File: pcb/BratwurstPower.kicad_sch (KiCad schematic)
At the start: 36 parts, among them J1 BarrelJack, J10 GPIO, J2 Raspi, J3 USB1in, J4 USB1out, J5 I2C, J6 I2C, J7 USB2in, J8 USB2out, J9 EXT, Q1 AO3401A, U1 PCA9557PW

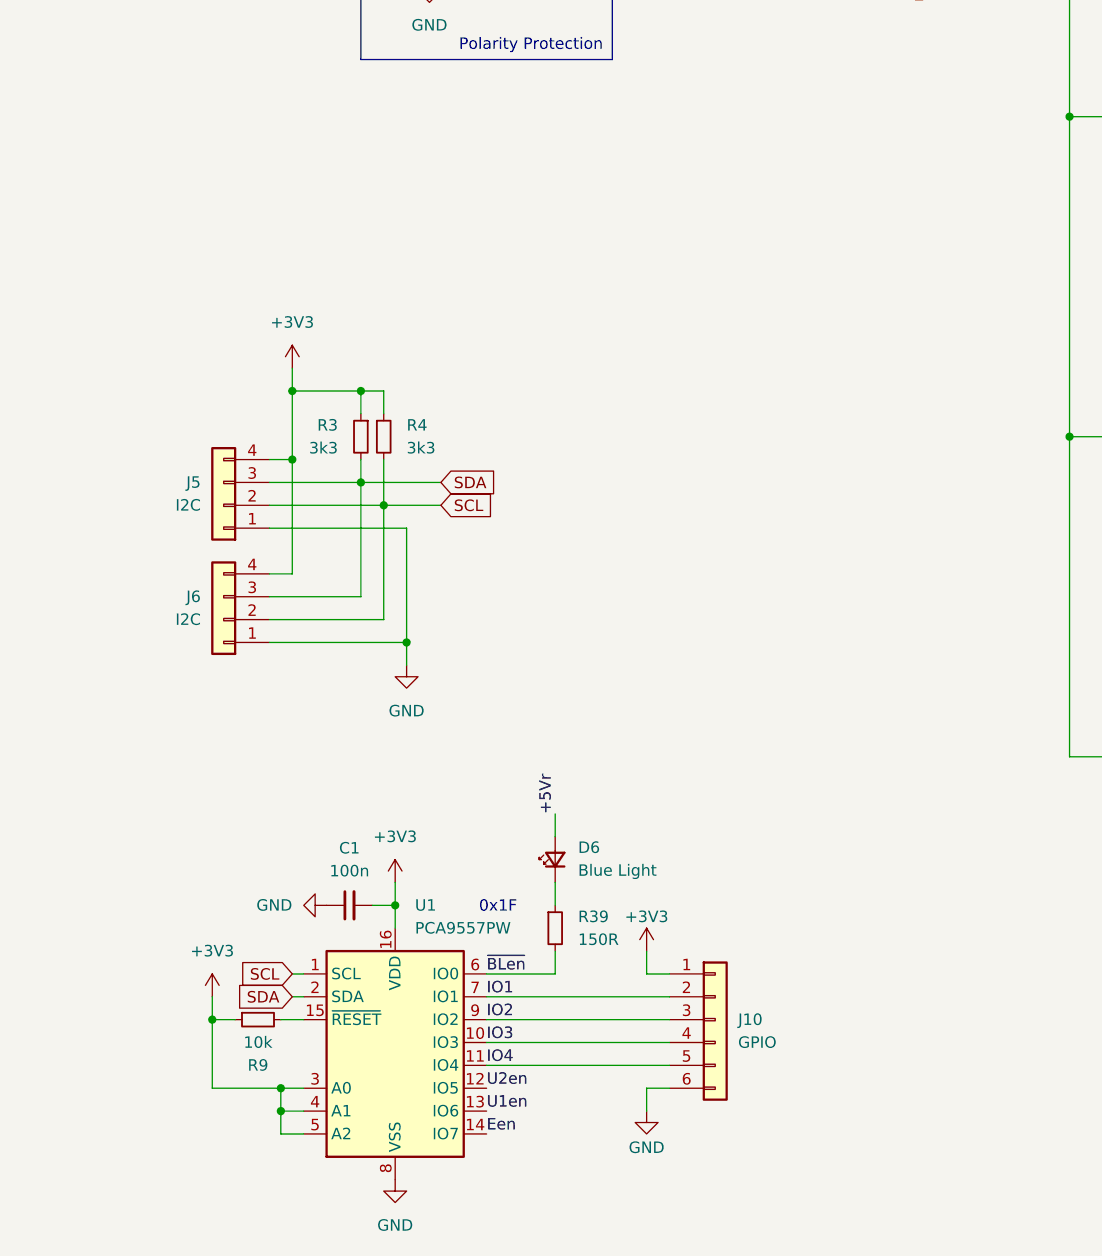
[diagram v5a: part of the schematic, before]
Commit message: fix: I2C pull-up strength
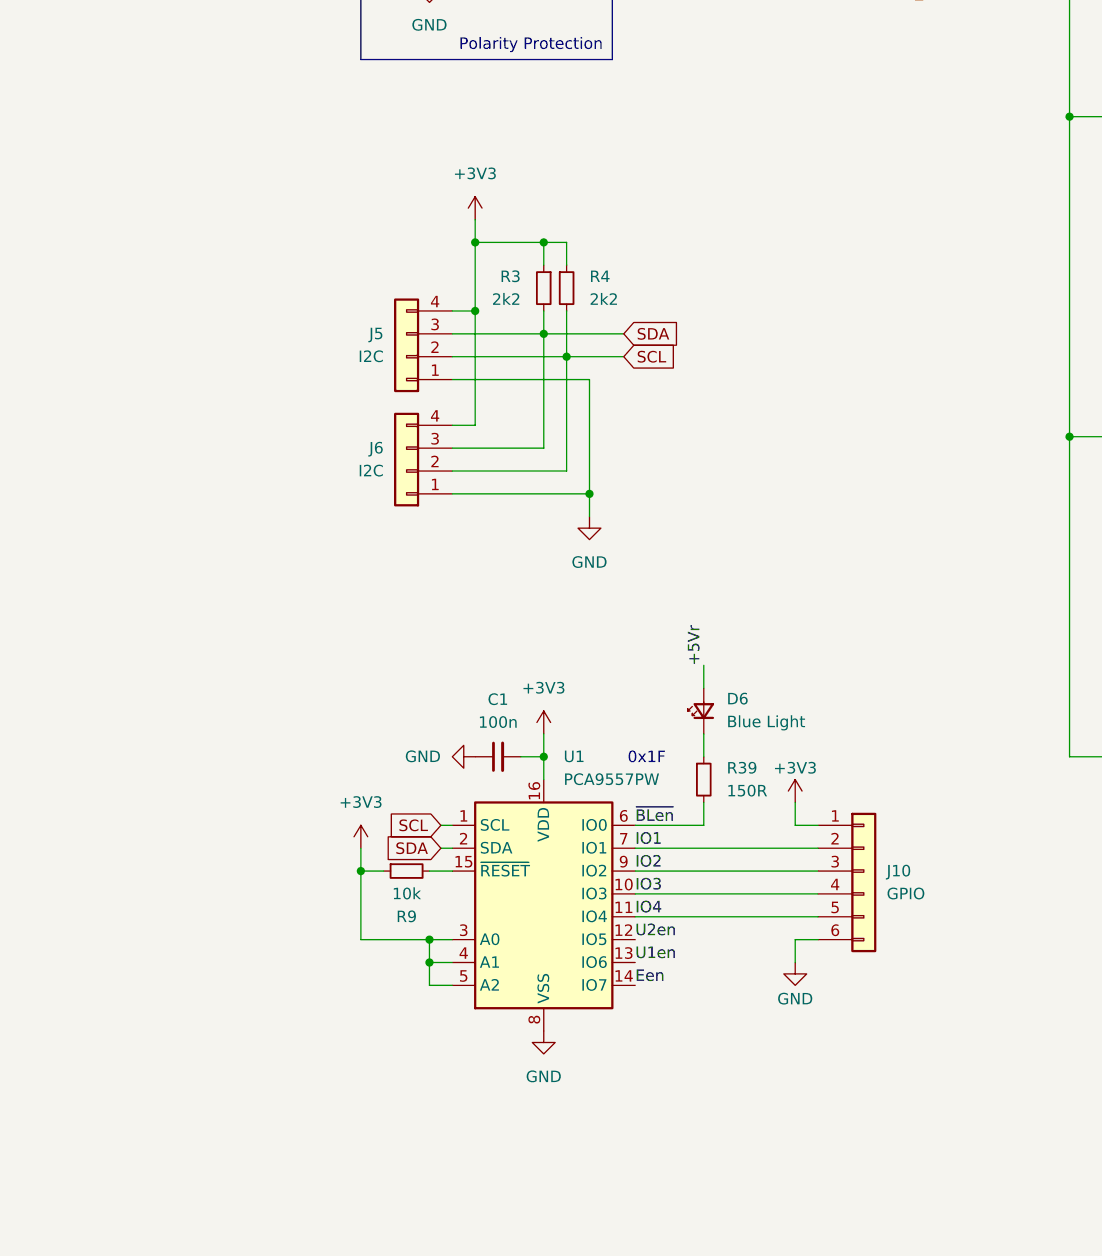
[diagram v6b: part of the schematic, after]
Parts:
- R3, R4: value 3k3 -> 2k2
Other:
- moved on the sheet: C1, D6, J10, J5, J6, R3, R39, R4, R9, U1

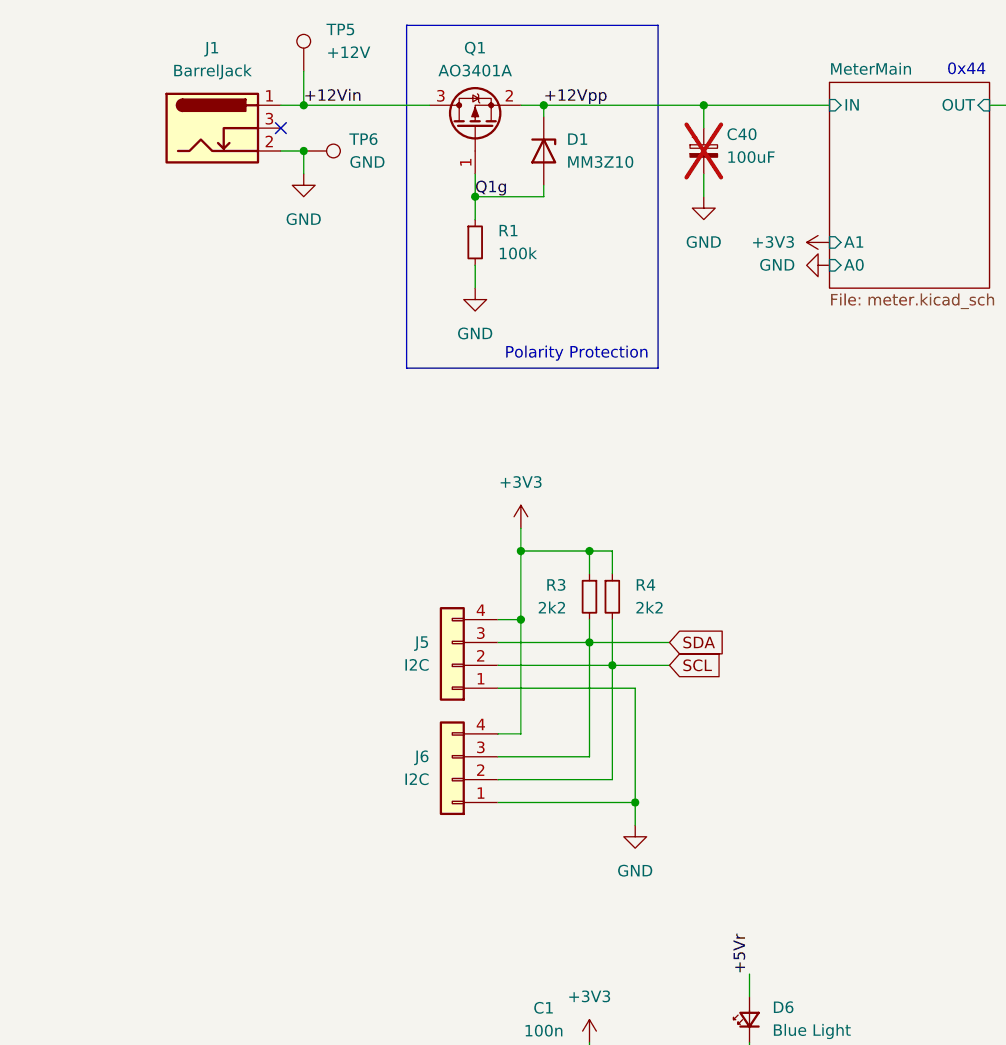
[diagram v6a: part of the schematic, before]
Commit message: feat: polarity protection for I2C bus
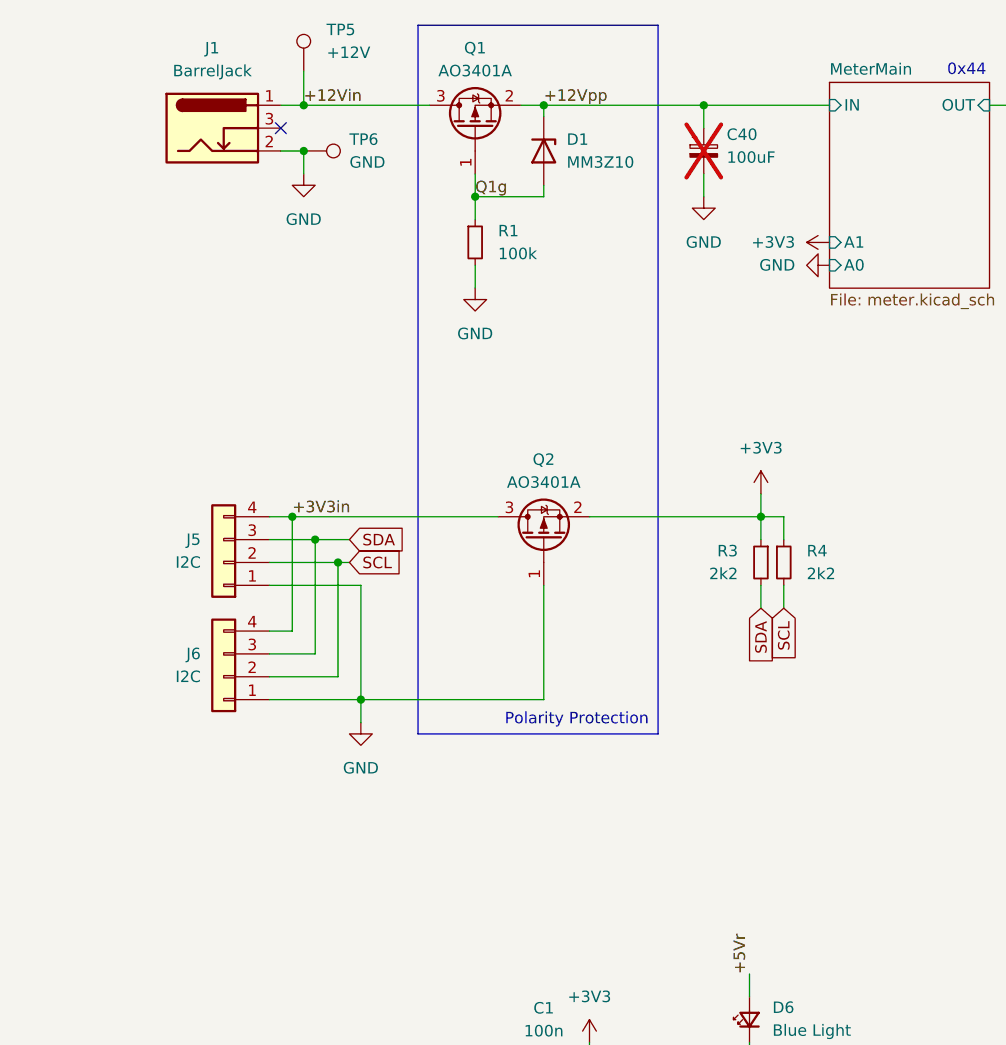
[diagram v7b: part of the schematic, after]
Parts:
- added Q2: AO3401A, Package_TO_SOT_SMD:SOT-23, symbol Transistor_FET:AO3401A
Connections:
- net +3V3: now also Q2.2 (S); no longer J5.4 (Pin_4), J6.4 (Pin_4)
- net GND: now also Q2.1 (G)
- new net +3V3in: J5.4 (Pin_4), J6.4 (Pin_4), Q2.3 (D)
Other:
- moved on the sheet: J5, J6, R3, R4

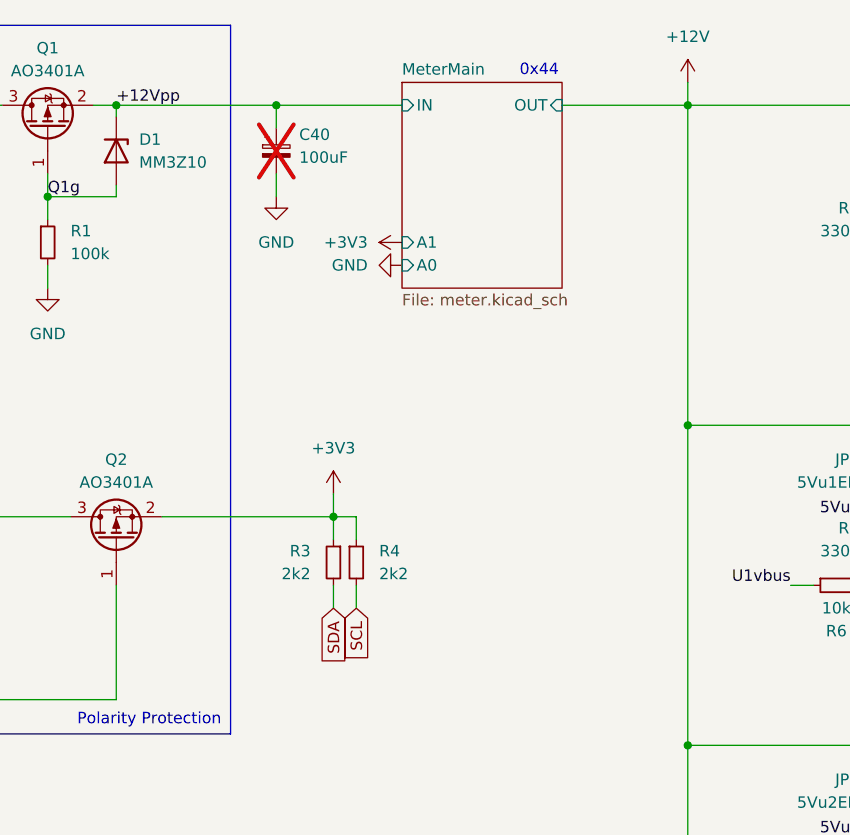
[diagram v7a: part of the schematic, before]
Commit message: fix: add capacitor to 3V3 rail
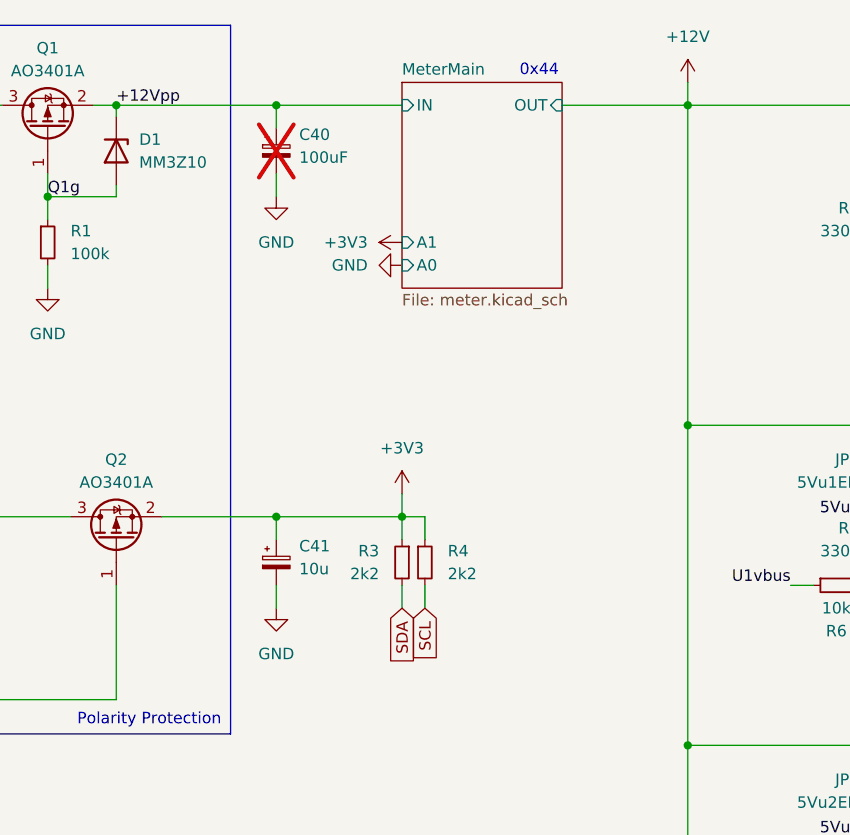
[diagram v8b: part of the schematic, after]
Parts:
- added C41: 10u, Capacitor_Tantalum_SMD:CP_EIA-3216-18_Kemet-A, symbol Device:C_Polarized_Small
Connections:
- net +3V3: now also C41.1
- net GND: now also C41.2
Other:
- moved on the sheet: R3, R4
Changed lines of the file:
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@@
 	)
 	(junction
+		(at 76.2 74.93)
+		(diameter 0)
+		(color 0 0 0 0)
+	)
+	(junction
 		(at 121.92 64.77)
 		(diameter 0)
@@
 	)
 	(junction
-		(at 82.55 74.93)
+		(at 90.17 74.93)
 		(diameter 0)
 		(color 0 0 0 0)
@@
 	(wire
 		(pts
-			(xy 82.55 74.93) (xy 82.55 77.47)
+			(xy 90.17 74.93) (xy 90.17 77.47)
 		)
 		(stroke
@@
 	(wire
 		(pts
+			(xy 76.2 82.55) (xy 76.2 85.09)
+		)
+		(stroke
+			(width 0)
+			(type default)
+		)
+	)
+	(wire
+		(pts
 			(xy 233.68 34.29) (xy 233.68 36.83)
 		)
@@
 	(wire
 		(pts
+			(xy 76.2 74.93) (xy 90.17 74.93)
+		)
+		(stroke
+			(width 0)
+			(type default)
+		)
+	)
+	(wire
+		(pts
 			(xy 215.9 81.28) (xy 215.9 82.55)
 		)
@@
 	(wire
 		(pts
-			(xy 121.92 64.77) (xy 121.92 29.21)
+			(xy 121.92 29.21) (xy 121.92 64.77)
 		)
 		(stroke
@@
 	(wire
 		(pts
-			(xy 82.55 82.55) (xy 82.55 85.09)
+			(xy 90.17 82.55) (xy 90.17 85.09)
 		)
 		(stroke
@@
 	(wire
 		(pts
+			(xy 76.2 74.93) (xy 76.2 77.47)
+		)
+		(stroke
+			(width 0)
+			(type default)
+		)
+	)
+	(wire
+		(pts
 			(xy 58.42 30.48) (xy 58.42 29.21)
 		)
@@
 	(wire
 		(pts
-			(xy 82.55 72.39) (xy 82.55 74.93)
+			(xy 90.17 72.39) (xy 90.17 74.93)
 		)
 		(stroke
@@
 	(wire
 		(pts
-			(xy 63.5 74.93) (xy 82.55 74.93)
+			(xy 63.5 74.93) (xy 76.2 74.93)
 		)
 		(stroke
@@
 	(wire
 		(pts
-			(xy 85.09 74.93) (xy 85.09 77.47)
+			(xy 92.71 74.93) (xy 92.71 77.47)
 		)
 		(stroke
@@
 	(wire
 		(pts
-			(xy 85.09 82.55) (xy 85.09 85.09)
+			(xy 92.71 82.55) (xy 92.71 85.09)
 		)
 		(stroke
@@
 	(wire
 		(pts
-			(xy 85.09 74.93) (xy 82.55 74.93)
+			(xy 92.71 74.93) (xy 90.17 74.93)
 		)
 		(stroke
@@
 	(global_label "SDA"
 		(shape input)
-		(at 82.55 85.09 270)
+		(at 90.17 85.09 270)
 		(fields_autoplaced yes)
 		(effects
@@
 		)
 		(property "Intersheetrefs" "${INTERSHEET_REFS}"
-			(at 82.55 91.6433 90)
+			(at 90.17 91.6433 90)
 			(effects
 				(font
@@
 	(global_label "SCL"
 		(shape input)
-		(at 85.09 85.09 270)
+		(at 92.71 85.09 270)
 		(fields_autoplaced yes)
 		(effects
@@
 		)
 		(property "Intersheetrefs" "${INTERSHEET_REFS}"
-			(at 85.09 91.5828 90)
+			(at 92.71 91.5828 90)
 			(effects
 				(font
@@
 	(symbol
 		(lib_id "power:+3V3")
-		(at 82.55 72.39 0)
+		(at 90.17 72.39 0)
 		(unit 1)
 		(exclude_from_sim no)
@@
 		(fields_autoplaced yes)
 		(property "Reference" "#PWR06"
-			(at 82.55 76.2 0)
+			(at 90.17 76.2 0)
 			(effects
 				(font
@@
 		)
 		(property "Value" "+3V3"
-			(at 82.55 67.31 0)
+			(at 90.17 67.31 0)
 			(effects
 				(font
@@
 		)
 		(property "Footprint" ""
-			(at 82.55 72.39 0)
+			(at 90.17 72.39 0)
 			(effects
 				(font
@@
 		)
 		(property "Datasheet" ""
-			(at 82.55 72.39 0)
+			(at 90.17 72.39 0)
 			(effects
 				(font
@@
 		)
 		(property "Description" "Power symbol creates a global label with name \"+3V3\""
-			(at 82.55 72.39 0)
+			(at 90.17 72.39 0)
 			(effects
 				(font
@@
 	)
 	(symbol
+		(lib_id "Device:C_Polarized_Small")
+		(at 76.2 80.01 0)
+		(unit 1)
+		(exclude_from_sim no)
+		(in_bom yes)
+		(on_board yes)
+		(dnp no)
+		(fields_autoplaced yes)
+		(property "Reference" "C41"
+			(at 78.74 78.1938 0)
+			(effects
+				(font
+					(size 1.27 1.27)
+				)
+				(justify left)
+			)
+		)
+		(property "Value" "10u"
+			(at 78.74 80.7338 0)
+			(effects
+				(font
+					(size 1.27 1.27)
+				)
+				(justify left)
+			)
+		)
+		(property "Footprint" "Capacitor_Tantalum_SMD:CP_EIA-3216-18_Kemet-A"
+			(at 76.2 80.01 0)
+			(effects
+				(font
+					(size 1.27 1.27)
+				)
+				(hide yes)
+			)
+		)
+		(property "Datasheet" "~"
+			(at 76.2 80.01 0)
+			(effects
+				(font
+					(size 1.27 1.27)
+				)
+				(hide yes)
+			)
+		)
+		(property "Description" "Polarized capacitor, small symbol"
+			(at 76.2 80.01 0)
+			(effects
+				(font
+					(size 1.27 1.27)
+				)
+				(hide yes)
+			)
+		)
+		(pin "2"
+		)
+		(pin "1"
+		)
+		(instances
+			(project ""
+				(path "/d3b20f0a-e666-4f64-bba3-6679d961a6dd"
+					(reference "C41")
+					(unit 1)
+				)
+			)
+		)
+	)
+	(symbol
 		(lib_id "power:PWR_FLAG")
 		(at -20.32 162.56 180)
@@
 	)
 	(symbol
+		(lib_id "power:GND")
+		(at 76.2 85.09 0)
+		(unit 1)
+		(exclude_from_sim no)
+		(in_bom yes)
+		(on_board yes)
+		(dnp no)
+		(fields_autoplaced yes)
+		(property "Reference" "#PWR048"
+			(at 76.2 91.44 0)
+			(effects
+				(font
+					(size 1.27 1.27)
+				)
+				(hide yes)
+			)
+		)
+		(property "Value" "GND"
+			(at 76.2 90.17 0)
+			(effects
+				(font
+					(size 1.27 1.27)
+				)
+			)
+		)
+		(property "Footprint" ""
+			(at 76.2 85.09 0)
+			(effects
+				(font
+					(size 1.27 1.27)
+				)
+				(hide yes)
+			)
+		)
+		(property "Datasheet" ""
+			(at 76.2 85.09 0)
+			(effects
+				(font
+					(size 1.27 1.27)
+				)
+				(hide yes)
+			)
+		)
+		(property "Description" "Power symbol creates a global label with name \"GND\" , ground"
+			(at 76.2 85.09 0)
+			(effects
+				(font
+					(size 1.27 1.27)
+				)
+				(hide yes)
+			)
+		)
+		(pin "1"
+		)
+		(instances
+			(project "BratwurstPower"
+				(path "/d3b20f0a-e666-4f64-bba3-6679d961a6dd"
+					(reference "#PWR048")
+					(unit 1)
+				)
+			)
+		)
+	)
+	(symbol
 		(lib_id "Connector:USB_A")
 		(at 243.84 34.29 0)
@@
 	(symbol
 		(lib_id "Device:R_Small")
-		(at 85.09 80.01 0)
+		(at 92.71 80.01 0)
 		(unit 1)
 		(exclude_from_sim no)
@@
 		(fields_autoplaced yes)
 		(property "Reference" "R4"
-			(at 87.63 78.7399 0)
+			(at 95.25 78.7399 0)
 			(effects
 				(font
@@
 		)
 		(property "Value" "2k2"
-			(at 87.63 81.2799 0)
+			(at 95.25 81.2799 0)
 			(effects
 				(font
@@
 		)
 		(property "Footprint" "Resistor_SMD:R_0402_1005Metric"
-			(at 85.09 80.01 0)
+			(at 92.71 80.01 0)
 			(effects
 				(font
@@
 		)
 		(property "Datasheet" "~"
-			(at 85.09 80.01 0)
+			(at 92.71 80.01 0)
 			(effects
 				(font
@@
 		)
 		(property "Description" "Resistor, small symbol"
-			(at 85.09 80.01 0)
+			(at 92.71 80.01 0)
 			(effects
 				(font
@@
 		)
 		(property "LCSC" "C25890"
-			(at 85.09 80.01 0)
+			(at 92.71 80.01 0)
 			(effects
 				(font
@@
 	(symbol
 		(lib_id "Device:R_Small")
-		(at 82.55 80.01 0)
+		(at 90.17 80.01 0)
 		(mirror y)
 		(unit 1)
@@
 		(on_board yes)
 		(dnp no)
+		(fields_autoplaced yes)
 		(property "Reference" "R3"
-			(at 80.01 78.7399 0)
+			(at 87.63 78.7399 0)
 			(effects
 				(font
@@
 		)
 		(property "Value" "2k2"
-			(at 80.01 81.2799 0)
+			(at 87.63 81.2799 0)
 			(effects
 				(font
@@
 		)
 		(property "Footprint" "Resistor_SMD:R_0402_1005Metric"
-			(at 82.55 80.01 0)
+			(at 90.17 80.01 0)
 			(effects
 				(font
@@
 		)
 		(property "Datasheet" "~"
-			(at 82.55 80.01 0)
+			(at 90.17 80.01 0)
 			(effects
 				(font
@@
 		)
 		(property "Description" "Resistor, small symbol"
-			(at 82.55 80.01 0)
+			(at 90.17 80.01 0)
 			(effects
 				(font
@@
 		)
 		(property "LCSC" "C25890"
-			(at 82.55 80.01 0)
+			(at 90.17 80.01 0)
 			(effects
 				(font
